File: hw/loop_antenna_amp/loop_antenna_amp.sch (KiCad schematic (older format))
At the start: 87 parts, among them J1 ANT1, J2 ANT2, J3 GND, J4 Coax (SMA), Q1 MMBT3904, Q2 MMBT3904, Q3 MMBT3904, Q4 MMBT3904, Q5 PZT3904, Q6 PZT3904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

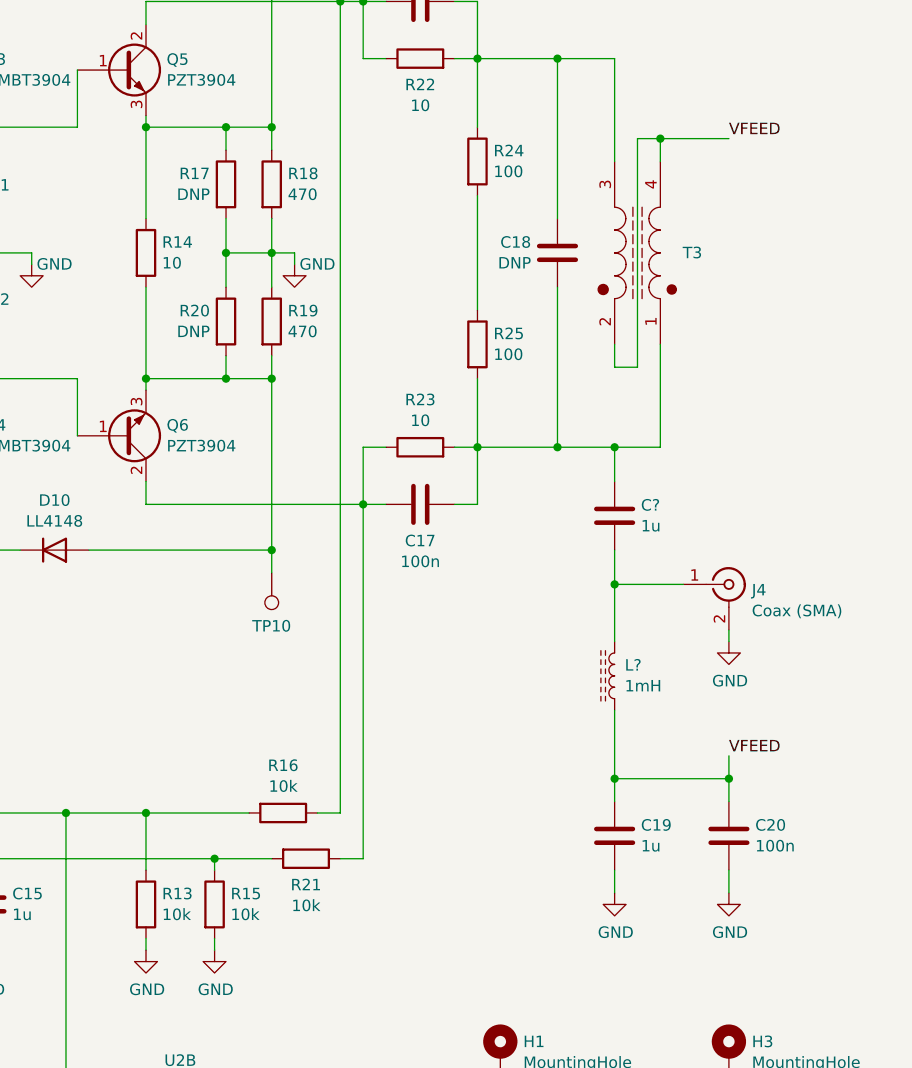
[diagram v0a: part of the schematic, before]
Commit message: Loop antenna amp: reannotate schematic, use bigger footprint for film caps
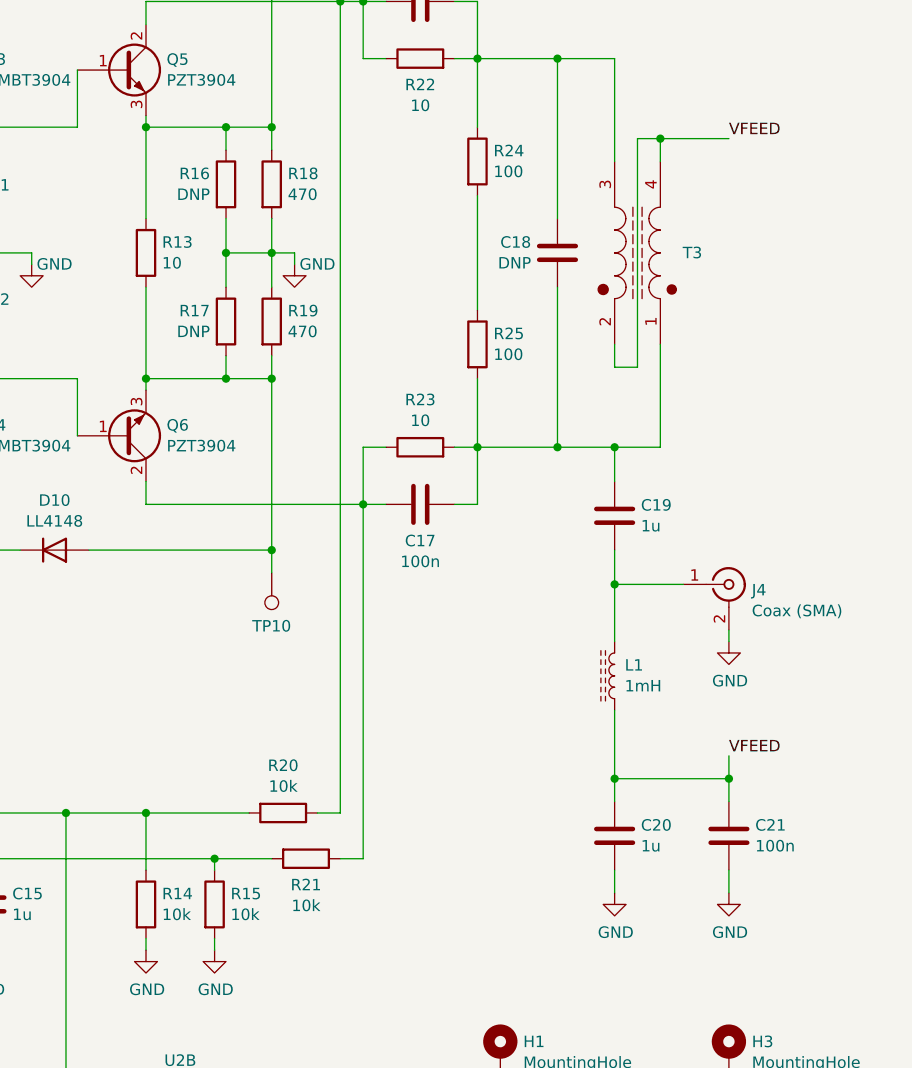
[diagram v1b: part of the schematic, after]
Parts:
- C14, C15: footprint Capacitor_THT:C_Rect_L7.0mm_W4.5mm_P5.00mm -> Capacitor_THT:C_Rect_L7.2mm_W5.5mm_P5.00mm_FKS2_FKP2_MKS2_MKP2
- C20: renamed from C19; footprint Capacitor_THT:C_Rect_L7.0mm_W4.5mm_P5.00mm -> Capacitor_THT:C_Rect_L7.2mm_W5.5mm_P5.00mm_FKS2_FKP2_MKS2_MKP2
- gave numbers to parts that had none: 2
- renumbered C20 to C21, R14 to R13, R13 to R14, R17 to R16, R20 to R17, R16 to R20
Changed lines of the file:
@@
 $EndComp
 $Comp
-L Device:R R14
+L Device:R R13
 U 1 1 60D4BDE0
 P 7950 2200
-F 0 "R14" H 8020 2246 50  0000 L CNN
+F 0 "R13" H 8020 2246 50  0000 L CNN
 F 1 "10" H 8020 2155 50  0000 L CNN
 F 2 "Resistor_SMD:R_0805_2012Metric_Pad1.15x1.40mm_HandSolder" V 7880 2200 50  0001 C CNN
@@
 	10000 4900 10000 5000
 $Comp
-L power:GND #PWR033
+L power:GND #PWR032
 U 1 1 60DD2FFC
 P 10000 5000
-F 0 "#PWR033" H 10000 4750 50  0001 C CNN
+F 0 "#PWR032" H 10000 4750 50  0001 C CNN
 F 1 "GND" H 10005 4827 50  0000 C CNN
 F 2 "" H 10000 5000 50  0001 C CNN
@@
 	10000 2700 10100 2700
 $Comp
-L Device:C C19
+L Device:C C20
 U 1 1 60DC0ECC
 P 10000 4750
-F 0 "C19" H 10115 4796 50  0000 L CNN
+F 0 "C20" H 10115 4796 50  0000 L CNN
 F 1 "1u" H 10115 4705 50  0000 L CNN
-F 2 "Capacitor_THT:C_Rect_L7.0mm_W4.5mm_P5.00mm" H 10038 4600 50  0001 C CNN
+F 2 "Capacitor_THT:C_Rect_L7.2mm_W5.5mm_P5.00mm_FKS2_FKP2_MKS2_MKP2" H 10038 4600 50  0001 C CNN
 F 3 "~" H 10000 4750 50  0001 C CNN
 	1    10000 4750
@@
 $EndComp
 $Comp
-L Device:R R16
+L Device:R R20
 U 1 1 611E2283
 P 8550 4650
-F 0 "R16" V 8343 4650 50  0000 C CNN
+F 0 "R20" V 8343 4650 50  0000 C CNN
 F 1 "10k" V 8434 4650 50  0000 C CNN
 F 2 "Resistor_SMD:R_0805_2012Metric_Pad1.15x1.40mm_HandSolder" V 8480 4650 50  0001 C CNN
@@
 Connection ~ 5500 6650
 $Comp
-L Device:C C20
+L Device:C C21
 U 1 1 617CFBCA
 P 10500 4750
-F 0 "C20" H 10615 4796 50  0000 L CNN
+F 0 "C21" H 10615 4796 50  0000 L CNN
 F 1 "100n" H 10615 4705 50  0000 L CNN
 F 2 "Capacitor_SMD:C_0805_2012Metric_Pad1.15x1.40mm_HandSolder" H 10538 4600 50  0001 C CNN
@@
 $EndComp
 $Comp
-L power:GND #PWR035
+L power:GND #PWR033
 U 1 1 60DDA9B5
 P 10500 3900
-F 0 "#PWR035" H 10500 3650 50  0001 C CNN
+F 0 "#PWR033" H 10500 3650 50  0001 C CNN
 F 1 "GND" H 10505 3727 50  0000 C CNN
 F 2 "" H 10500 3900 50  0001 C CNN
@@
 Connection ~ 7950 4650
 $Comp
-L Device:R R13
+L Device:R R14
 U 1 1 620D89BD
 P 7950 5050
-F 0 "R13" H 8020 5096 50  0000 L CNN
+F 0 "R14" H 8020 5096 50  0000 L CNN
 F 1 "10k" H 8020 5005 50  0000 L CNN
 F 2 "Resistor_SMD:R_0805_2012Metric_Pad1.15x1.40mm_HandSolder" V 7880 5050 50  0001 C CNN
@@
 F 0 "C15" H 7365 5096 50  0000 L CNN
 F 1 "1u" H 7365 5005 50  0000 L CNN
-F 2 "Capacitor_THT:C_Rect_L7.0mm_W4.5mm_P5.00mm" H 7288 4900 50  0001 C CNN
+F 2 "Capacitor_THT:C_Rect_L7.2mm_W5.5mm_P5.00mm_FKS2_FKP2_MKS2_MKP2" H 7288 4900 50  0001 C CNN
 F 3 "~" H 7250 5050 50  0001 C CNN
 	1    7250 5050
@@
 F 0 "C14" V 6548 4300 50  0000 C CNN
 F 1 "1u" V 6639 4300 50  0000 C CNN
-F 2 "Capacitor_THT:C_Rect_L7.0mm_W4.5mm_P5.00mm" H 6838 4150 50  0001 C CNN
+F 2 "Capacitor_THT:C_Rect_L7.2mm_W5.5mm_P5.00mm_FKS2_FKP2_MKS2_MKP2" H 6838 4150 50  0001 C CNN
 F 3 "~" H 6800 4300 50  0001 C CNN
 	1    6800 4300
@@
 	4850 4750 4500 4750
 $Comp
-L Device:L_Core_Ferrite L?
+L Device:L_Core_Ferrite L1
 U 1 1 62533594
 P 10000 4050
-F 0 "L?" H 9956 4004 50  0000 R CNN
+F 0 "L1" H 9956 4004 50  0000 R CNN
 F 1 "1mH" H 9956 4095 50  0000 R CNN
 F 2 "Inductor_THT:L_Radial_D8.7mm_P5.00mm_Fastron_07HCP" H 10000 4050 50  0001 C CNN
@@
 $EndComp
 $Comp
-L Device:C C?
+L Device:C C19
 U 1 1 6254CA9B
 P 10000 3350
-F 0 "C?" H 9885 3304 50  0000 R CNN
+F 0 "C19" H 9885 3304 50  0000 R CNN
 F 1 "1u" H 9885 3395 50  0000 R CNN
 F 2 "Capacitor_THT:C_Rect_L7.2mm_W5.5mm_P5.00mm_FKS2_FKP2_MKS2_MKP2" H 10038 3200 50  0001 C CNN
@@
 	8300 2200 8300 2350
 $Comp
-L Device:R R20
+L Device:R R17
 U 1 1 624281D1
 P 8300 2500
-F 0 "R20" H 8230 2546 50  0000 R CNN
+F 0 "R17" H 8230 2546 50  0000 R CNN
 F 1 "DNP" H 8230 2455 50  0000 R CNN
 F 2 "Resistor_SMD:R_0805_2012Metric_Pad1.15x1.40mm_HandSolder" V 8230 2500 50  0001 C CNN
@@
 	8300 1750 8300 1650
 $Comp
-L Device:R R17
+L Device:R R16
 U 1 1 624079CA
 P 8300 1900
-F 0 "R17" H 8230 1946 50  0000 R CNN
+F 0 "R16" H 8230 1946 50  0000 R CNN
 F 1 "DNP" H 8230 1855 50  0000 R CNN
 F 2 "Resistor_SMD:R_0805_2012Metric_Pad1.15x1.40mm_HandSolder" V 8230 1900 50  0001 C CNN

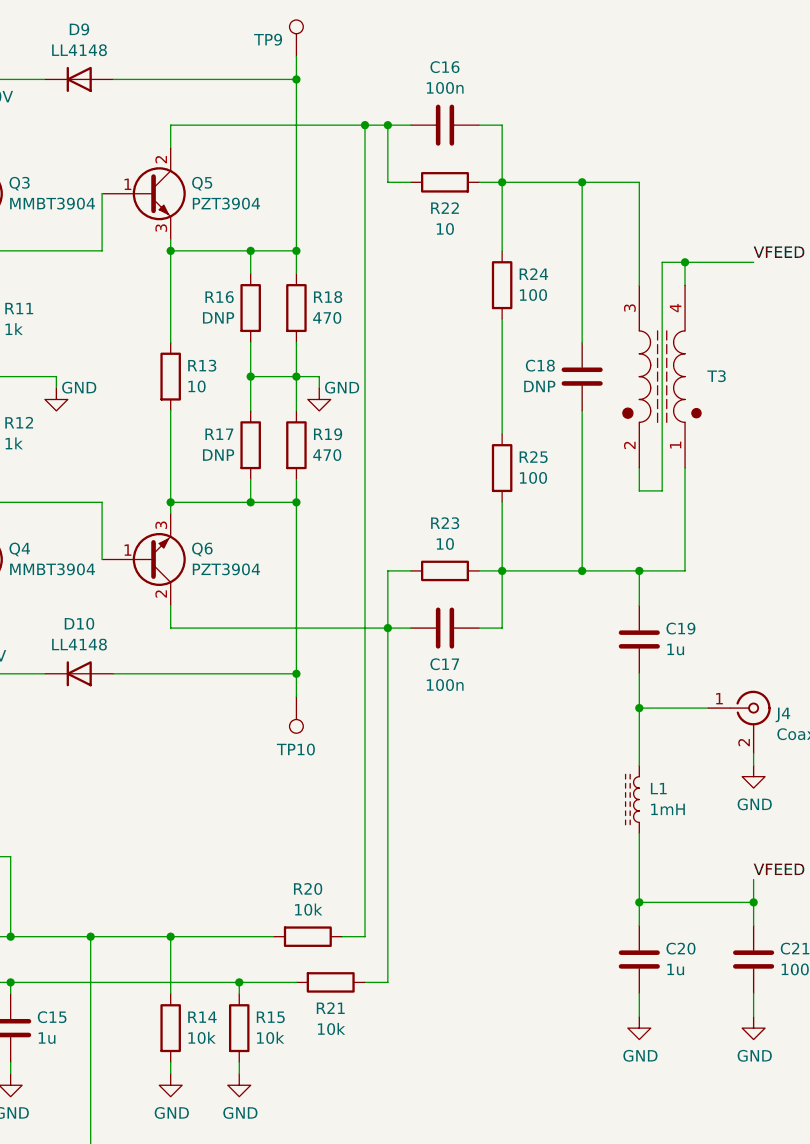
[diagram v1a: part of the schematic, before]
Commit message: Loop antenna amp: update PCB to match schematic
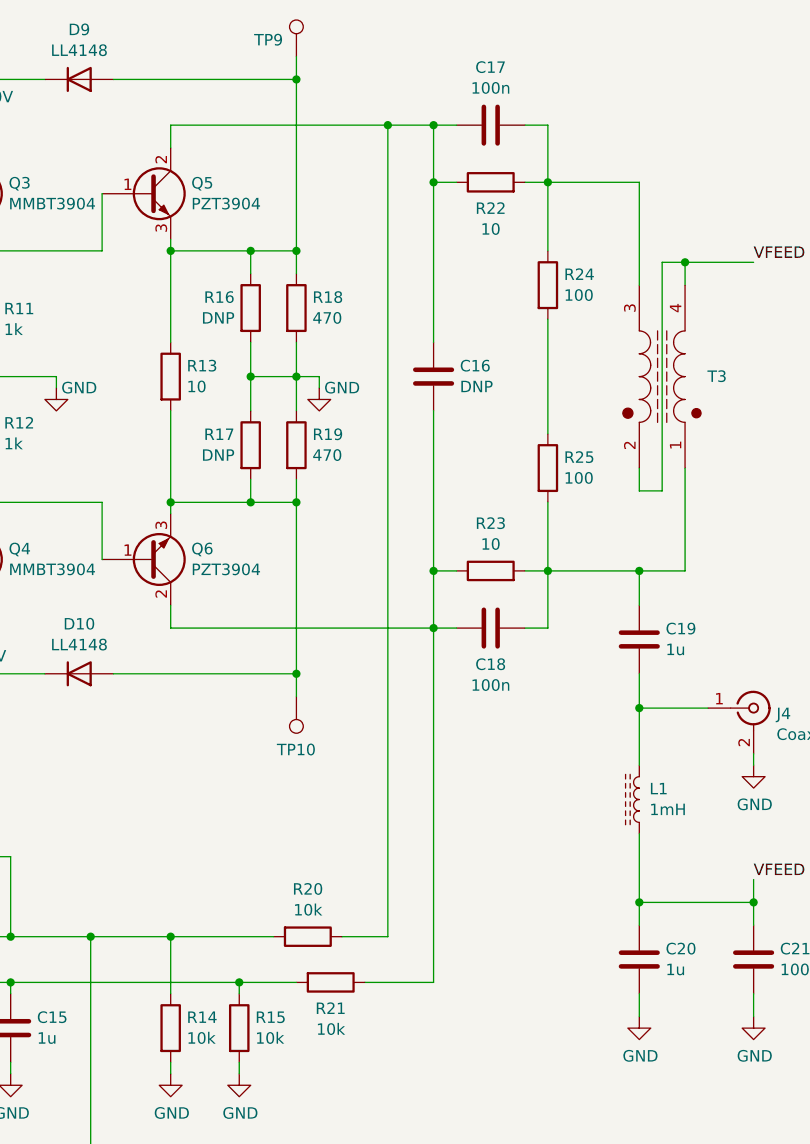
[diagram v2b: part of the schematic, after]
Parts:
- renumbered C18 to C16, C16 to C17, C17 to C18
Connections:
- net at C17.2, Q5.2 (C), Q5.4 (C)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: now also C16.1
- net at C18.2, Q6.2 (C), Q6.4 (C)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: now also C16.2
- net at C17.1, R22.2, R24.1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: no longer C16.1
- net at C18.1, C19.2, R23.2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: no longer C16.2
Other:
- moved on the sheet: C16, C17, C18, R22, R23, R24, R25
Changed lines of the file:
@@
 Wire Wire Line
 	10200 3050 10200 2600
-Connection ~ 9750 3050
 $Comp
 L local_syms:Transformer_TL_Basic T3
@@
 	0    1    -1   0
 $EndComp
-Connection ~ 9400 3050
-Wire Wire Line
-	9750 2350 9750 3050
-Connection ~ 9400 1350
-$Comp
-L Device:C C18
+Connection ~ 9600 3050
+Connection ~ 9600 1350
+$Comp
+L Device:C C16
 U 1 1 60D72AEE
-P 9750 2200
-F 0 "C18" H 9635 2246 50  0000 R CNN
-F 1 "DNP" H 9635 2155 50  0000 R CNN
-F 2 "Capacitor_SMD:C_0805_2012Metric_Pad1.15x1.40mm_HandSolder" H 9788 2050 50  0001 C CNN
-F 3 "~" H 9750 2200 50  0001 C CNN
-	1    9750 2200
-	1    0    0    -1
-$EndComp
-Wire Wire Line
-	9400 1950 9400 2450
-Wire Wire Line
-	9400 3050 9400 2750
-Wire Wire Line
-	9400 1350 9400 1650
+P 9100 2200
+F 0 "C16" H 9215 2246 50  0000 L CNN
+F 1 "DNP" H 9215 2155 50  0000 L CNN
+F 2 "Capacitor_SMD:C_0805_2012Metric_Pad1.15x1.40mm_HandSolder" H 9138 2050 50  0001 C CNN
+F 3 "~" H 9100 2200 50  0001 C CNN
+	1    9100 2200
+	1    0    0    -1
+$EndComp
+Wire Wire Line
+	9600 1950 9600 2450
+Wire Wire Line
+	9600 3050 9600 2750
+Wire Wire Line
+	9600 1350 9600 1650
 $Comp
 L Device:R R25
 U 1 1 60D6B31A
-P 9400 2600
-F 0 "R25" H 9470 2646 50  0000 L CNN
-F 1 "100" H 9470 2555 50  0000 L CNN
-F 2 "Resistor_SMD:R_0805_2012Metric_Pad1.15x1.40mm_HandSolder" V 9330 2600 50  0001 C CNN
-F 3 "~" H 9400 2600 50  0001 C CNN
-	1    9400 2600
+P 9600 2600
+F 0 "R25" H 9670 2646 50  0000 L CNN
+F 1 "100" H 9670 2555 50  0000 L CNN
+F 2 "Resistor_SMD:R_0805_2012Metric_Pad1.15x1.40mm_HandSolder" V 9530 2600 50  0001 C CNN
+F 3 "~" H 9600 2600 50  0001 C CNN
+	1    9600 2600
 	1    0    0    -1
 $EndComp
@@
 L Device:R R24
 U 1 1 60D5D69E
-P 9400 1800
-F 0 "R24" H 9470 1846 50  0000 L CNN
-F 1 "100" H 9470 1755 50  0000 L CNN
-F 2 "Resistor_SMD:R_0805_2012Metric_Pad1.15x1.40mm_HandSolder" V 9330 1800 50  0001 C CNN
-F 3 "~" H 9400 1800 50  0001 C CNN
-	1    9400 1800
+P 9600 1800
+F 0 "R24" H 9670 1846 50  0000 L CNN
+F 1 "100" H 9670 1755 50  0000 L CNN
+F 2 "Resistor_SMD:R_0805_2012Metric_Pad1.15x1.40mm_HandSolder" V 9530 1800 50  0001 C CNN
+F 3 "~" H 9600 1800 50  0001 C CNN
+	1    9600 1800
 	1    0    0    -1
 $EndComp
@@
 	10000 4600 10000 4500
 Wire Wire Line
-	9300 1350 9400 1350
-Wire Wire Line
-	9300 3050 9400 3050
+	9500 1350 9600 1350
+Wire Wire Line
+	9500 3050 9600 3050
 Wire Wire Line
 	8500 3500 8500 3600
@@
 	7700 3500 8500 3500
 $Comp
-L Device:C C17
+L Device:C C18
 U 1 1 62031FD0
-P 9150 3300
-F 0 "C17" V 9310 3300 50  0000 C CNN
-F 1 "100n" V 9401 3300 50  0000 C CNN
-F 2 "Capacitor_SMD:C_0805_2012Metric_Pad1.15x1.40mm_HandSolder" H 9188 3150 50  0001 C CNN
-F 3 "~" H 9150 3300 50  0001 C CNN
-	1    9150 3300
+P 9350 3300
+F 0 "C18" V 9510 3300 50  0000 C CNN
+F 1 "100n" V 9601 3300 50  0000 C CNN
+F 2 "Capacitor_SMD:C_0805_2012Metric_Pad1.15x1.40mm_HandSolder" H 9388 3150 50  0001 C CNN
+F 3 "~" H 9350 3300 50  0001 C CNN
+	1    9350 3300
 	0    1    1    0
 $EndComp
 Wire Wire Line
-	9000 3300 8900 3300
-Wire Wire Line
-	8900 3300 8900 3050
-Wire Wire Line
-	8900 3050 9000 3050
-Wire Wire Line
-	9300 3300 9400 3300
-Wire Wire Line
-	9400 3300 9400 3050
-Wire Wire Line
-	8900 1350 8900 1100
-Wire Wire Line
-	8900 1100 9000 1100
-Wire Wire Line
-	9400 1100 9400 1350
-Wire Wire Line
-	9300 1100 9400 1100
-Wire Wire Line
-	8900 1350 9000 1350
-Wire Wire Line
-	9400 3050 9750 3050
+	9200 3300 9100 3300
+Wire Wire Line
+	9100 3300 9100 3050
+Wire Wire Line
+	9100 3050 9200 3050
+Wire Wire Line
+	9500 3300 9600 3300
+Wire Wire Line
+	9600 3300 9600 3050
+Wire Wire Line
+	9100 1350 9100 1100
+Wire Wire Line
+	9100 1100 9200 1100
+Wire Wire Line
+	9600 1100 9600 1350
+Wire Wire Line
+	9500 1100 9600 1100
+Wire Wire Line
+	9100 1350 9200 1350
 $Comp
 L power:GND #PWR029
@@
 Connection ~ 10000 3650
 Wire Wire Line
-	9750 3050 10000 3050
-Wire Wire Line
 	10000 4500 10500 4500
 Connection ~ 10000 3050
@@
 	7950 3200 7950 3300
 Wire Wire Line
-	7950 3300 8900 3300
-Connection ~ 8900 3300
+	7950 3300 9100 3300
+Connection ~ 9100 3300
 $Comp
 L Device:R R23
 U 1 1 61F23563
-P 9150 3050
-F 0 "R23" V 9357 3050 50  0000 C CNN
-F 1 "10" V 9266 3050 50  0000 C CNN
-F 2 "Resistor_SMD:R_0805_2012Metric_Pad1.15x1.40mm_HandSolder" V 9080 3050 50  0001 C CNN
-F 3 "~" H 9150 3050 50  0001 C CNN
-	1    9150 3050
+P 9350 3050
+F 0 "R23" V 9557 3050 50  0000 C CNN
+F 1 "10" V 9466 3050 50  0000 C CNN
+F 2 "Resistor_SMD:R_0805_2012Metric_Pad1.15x1.40mm_HandSolder" V 9280 3050 50  0001 C CNN
+F 3 "~" H 9350 3050 50  0001 C CNN
+	1    9350 3050
 	0    -1   -1   0
 $EndComp
@@
 Wire Wire Line
 	7950 1200 7950 1100
-Connection ~ 8900 1100
-Wire Wire Line
-	9750 2050 9750 1350
+Connection ~ 9100 1100
 Wire Wire Line
 	10000 1350 10000 1800
-Wire Wire Line
-	9750 1350 10000 1350
-Connection ~ 9750 1350
-Wire Wire Line
-	9750 1350 9400 1350
 $Comp
 L Device:R R22
 U 1 1 61F230EC
-P 9150 1350
-F 0 "R22" V 9035 1350 50  0000 C CNN
-F 1 "10" V 8944 1350 50  0000 C CNN
-F 2 "Resistor_SMD:R_0805_2012Metric_Pad1.15x1.40mm_HandSolder" V 9080 1350 50  0001 C CNN
-F 3 "~" H 9150 1350 50  0001 C CNN
-	1    9150 1350
+P 9350 1350
+F 0 "R22" V 9235 1350 50  0000 C CNN
+F 1 "10" V 9144 1350 50  0000 C CNN
+F 2 "Resistor_SMD:R_0805_2012Metric_Pad1.15x1.40mm_HandSolder" V 9280 1350 50  0001 C CNN
+F 3 "~" H 9350 1350 50  0001 C CNN
+	1    9350 1350
 	0    -1   -1   0
 $EndComp
 $Comp
-L Device:C C16
+L Device:C C17
 U 1 1 6206C7D0
-P 9150 1100
-F 0 "C16" V 8898 1100 50  0000 C CNN
-F 1 "100n" V 8989 1100 50  0000 C CNN
-F 2 "Capacitor_SMD:C_0805_2012Metric_Pad1.15x1.40mm_HandSolder" H 9188 950 50  0001 C CNN
-F 3 "~" H 9150 1100 50  0001 C CNN
-	1    9150 1100
+P 9350 1100
+F 0 "C17" V 9098 1100 50  0000 C CNN
+F 1 "100n" V 9189 1100 50  0000 C CNN
+F 2 "Capacitor_SMD:C_0805_2012Metric_Pad1.15x1.40mm_HandSolder" H 9388 950 50  0001 C CNN
+F 3 "~" H 9350 1100 50  0001 C CNN
+	1    9350 1100
 	0    1    1    0
 $EndComp
@@
 $EndComp
 Wire Wire Line
-	8800 1100 8900 1100
-Connection ~ 8800 1100
-Wire Wire Line
-	7950 1100 8800 1100
+	8900 1100 9100 1100
+Connection ~ 8900 1100
+Wire Wire Line
+	7950 1100 8900 1100
 $Comp
 L power:GND #PWR031
@@
 	8600 2200 8600 2250
 Wire Wire Line
-	8800 4850 8900 4850
+	8800 4850 9100 4850
 Wire Wire Line
 	8250 4850 8500 4850
 Wire Wire Line
-	8700 4650 8800 4650
-Wire Wire Line
-	8800 1100 8800 4650
-Wire Wire Line
-	8900 3300 8900 4850
+	8700 4650 8900 4650
+Wire Wire Line
+	8900 1100 8900 4650
+Wire Wire Line
+	9100 3300 9100 4850
+Wire Wire Line
+	9100 1350 9100 2050
+Connection ~ 9100 1350
+Wire Wire Line
+	9100 3050 9100 2350
+Connection ~ 9100 3050
+Wire Wire Line
+	9600 1350 10000 1350
+Wire Wire Line
+	9600 3050 10000 3050
 $EndSCHEMATC
